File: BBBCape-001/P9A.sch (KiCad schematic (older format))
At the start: 29 parts, among them J1 addr, J3 CONN_6, J4 CONN_3, J5 CONN_3, J7 CONN_3, J8 CONN_4, Q2 BSS138, Q3 BSS138, Q4 BSS138, Q7 BSS138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

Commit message: Got GVS hooked up
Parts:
- removed U2: CAT24C256, SO8E, symbol CAT24C256
- added U2: CAT24C256, SO8E, symbol 24C512
- BRD1: renamed from U?; footprint ~ -> BEAGLEBONE
- J1: value addr -> ADR SEL
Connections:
- net labels added: GNDA_ADC, VDD_ADC
- wire segments 124 -> 122
- no-connect marks 1 -> 0
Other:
- moved on the sheet: BRD1C, C1, J1, R3, R4, R5

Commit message: CAPE UPS
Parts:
- removed J3: CONN_6, PIN_ARRAY-6X1, symbol CONN_6
- added F1: FUSE, SM1206, symbol FUSE
- added J10, J11, J12, J3: CONN_3, PIN_ARRAY_3X1, symbol CONN_3
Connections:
- net labels added: VDD_5V-UF
- wire segments 122 -> 132
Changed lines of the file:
@@
-EESchema Schematic File Version 2  date 24/06/2014 16:39:12
+EESchema Schematic File Version 2  date 25/06/2014 16:57:40
 LIBS:power
 LIBS:device
@@
 Sheet 2 6
 Title "BeagleBone Cape Baseline"
-Date "24 jun 2014"
+Date "25 jun 2014"
 Rev "X1"
 Comp "Doug Gilliland <doug@douglasgilliland.com>"
@@
 SYS_5V
 Text Label 5000 1300 0    60   ~ 0
-VDD_5V
+VDD_5V-UF
 Text Label 5000 3200 0    60   ~ 0
 DGND_9_2
@@
 Text Notes 3350 6700 0    60   ~ 0
 G\nV\nS
-Text Label 2800 10050 0    60   ~ 0
+Text Label 8350 2400 0    60   ~ 0
 AIN0
-Text Label 2800 9950 0    60   ~ 0
+Text Label 8350 2050 0    60   ~ 0
 AIN2
-Text Label 2800 9850 0    60   ~ 0
+Text Label 8350 1350 0    60   ~ 0
 AIN6
-Text Label 2800 9750 0    60   ~ 0
+Text Label 8350 1700 0    60   ~ 0
 AIN4
 Wire Wire Line
@@
 Wire Wire Line
 	2750 6650 2750 6950
-Wire Wire Line
-	3300 10050 2650 10050
-Wire Wire Line
-	3300 9950 2650 9950
-Wire Wire Line
-	3300 9850 2650 9850
-Wire Wire Line
-	3300 9750 2650 9750
-Wire Wire Line
-	3300 10150 2650 10150
-Wire Wire Line
-	2650 9650 3300 9650
 Text Label 1250 8050 0    60   ~ 0
 UART4_RXD
@@
 GP117
 $Comp
-L CONN_6 J3
-U 1 1 53A86882
-P 3650 9900
-F 0 "J3" V 3600 9900 60  0000 C CNN
-F 1 "CONN_6" V 3700 9900 60  0000 C CNN
-F 2 "PIN_ARRAY-6X1" H 3650 9550 60  0000 C CNN
-F 3 "" H 3650 9900 60  0000 C CNN
-	1    3650 9900
-	1    0    0    -1
-$EndComp
-$Comp
 L BEAGLEBONEBLACK BRD1
 U 3 1 53A89A26
@@
 Connection ~ 2800 3900
 Text GLabel 5000 1300 0    60   UnSpc ~ 0
-VDD_5V
+VDD_5V-UF
 Text GLabel 5000 3300 0    60   UnSpc ~ 0
 GND
-Text GLabel 2650 9650 0    60   UnSpc ~ 0
+Text GLabel 8200 1250 0    60   UnSpc ~ 0
 VDD_ADC
-Text GLabel 2650 10150 0    60   UnSpc ~ 0
+Text GLabel 8200 2200 0    60   UnSpc ~ 0
 GNDA_ADC
-Text Label 2800 9650 0    60   ~ 0
+Text Label 8350 1250 0    60   ~ 0
 VDD_ADC
 Text GLabel 5000 1900 0    60   UnSpc ~ 0
 I2C1_SCL
-Text Label 2800 10150 0    60   ~ 0
+Text Label 8350 2200 0    60   ~ 0
 GNDA_ADC
+Text GLabel 5000 1400 0    60   UnSpc ~ 0
+SYS_5V
+Wire Wire Line
+	8200 1250 9150 1250
+Wire Wire Line
+	9150 2300 9050 2300
+Wire Wire Line
+	9050 2300 9050 1250
+Connection ~ 9050 1250
+Wire Wire Line
+	9150 1600 9050 1600
+Connection ~ 9050 1600
+Wire Wire Line
+	9150 1950 9050 1950
+Connection ~ 9050 1950
+Wire Wire Line
+	9150 1150 8950 1150
+Wire Wire Line
+	8200 2200 9150 2200
+Connection ~ 8950 2200
+Wire Wire Line
+	9150 1850 8950 1850
+Connection ~ 8950 1850
+Wire Wire Line
+	8950 1150 8950 2200
+Wire Wire Line
+	9150 1500 8950 1500
+Connection ~ 8950 1500
+Wire Wire Line
+	9150 1350 8200 1350
+Wire Wire Line
+	9150 1700 8200 1700
+Wire Wire Line
+	9150 2050 8200 2050
+Wire Wire Line
+	9150 2400 8200 2400
+$Comp
+L CONN_3 J3
+U 1 1 53AACBAD
+P 9500 1250
+F 0 "J3" V 9450 1250 50  0000 C CNN
+F 1 "CONN_3" V 9550 1250 40  0000 C CNN
+F 2 "PIN_ARRAY_3X1" H 9550 1000 60  0000 C CNN
+F 3 "" H 9500 1250 60  0000 C CNN
+	1    9500 1250
+	1    0    0    -1
+$EndComp
+$Comp
+L CONN_3 J10
+U 1 1 53AACBB3
+P 9500 1600
+F 0 "J10" V 9450 1600 50  0000 C CNN
+F 1 "CONN_3" V 9550 1600 40  0000 C CNN
+F 2 "PIN_ARRAY_3X1" H 9550 1350 60  0000 C CNN
+F 3 "" H 9500 1600 60  0000 C CNN
+	1    9500 1600
+	1    0    0    -1
+$EndComp
+$Comp
+L CONN_3 J11
+U 1 1 53AACBB9
+P 9500 1950
+F 0 "J11" V 9450 1950 50  0000 C CNN
+F 1 "CONN_3" V 9550 1950 40  0000 C CNN
+F 2 "PIN_ARRAY_3X1" H 9550 1700 60  0000 C CNN
+F 3 "" H 9500 1950 60  0000 C CNN
+	1    9500 1950
+	1    0    0    -1
+$EndComp
+$Comp
+L CONN_3 J12
+U 1 1 53AACBC9
+P 9500 2300
+F 0 "J12" V 9450 2300 50  0000 C CNN
+F 1 "CONN_3" V 9550 2300 40  0000 C CNN
+F 2 "PIN_ARRAY_3X1" H 9550 2050 60  0000 C CNN
+F 3 "" H 9500 2300 60  0000 C CNN
+	1    9500 2300
+	1    0    0    -1
+$EndComp
+Text GLabel 4100 2300 2    60   UnSpc ~ 0
+I2C2_SDA
+$Comp
+L FUSE F1
+U 1 1 53AAD570
+P 4350 800
+F 0 "F1" H 4450 850 40  0000 C CNN
+F 1 "FUSE" H 4250 750 40  0000 C CNN
+F 2 "SM1206" H 4350 650 60  0000 C CNN
+F 3 "~" H 4350 800 60  0000 C CNN
+	1    4350 800
+	1    0    0    -1
+$EndComp
+Text Label 4700 800  0    60   ~ 0
+VDD_5V-UF
+Text Label 3700 800  0    60   ~ 0
+VDD_5V
+Wire Wire Line
+	4600 800  5350 800
+Wire Wire Line
+	4100 800  3600 800
+Text GLabel 3600 800  0    60   UnSpc ~ 0
+VDD_5V
 $EndSCHEMATC

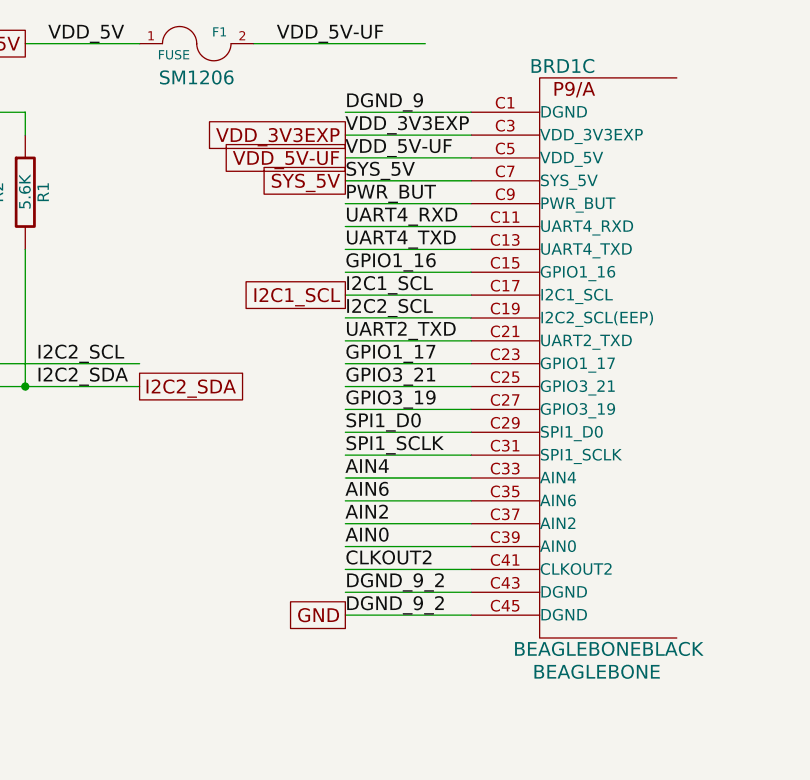
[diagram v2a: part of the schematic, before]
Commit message: New version, easier assembly
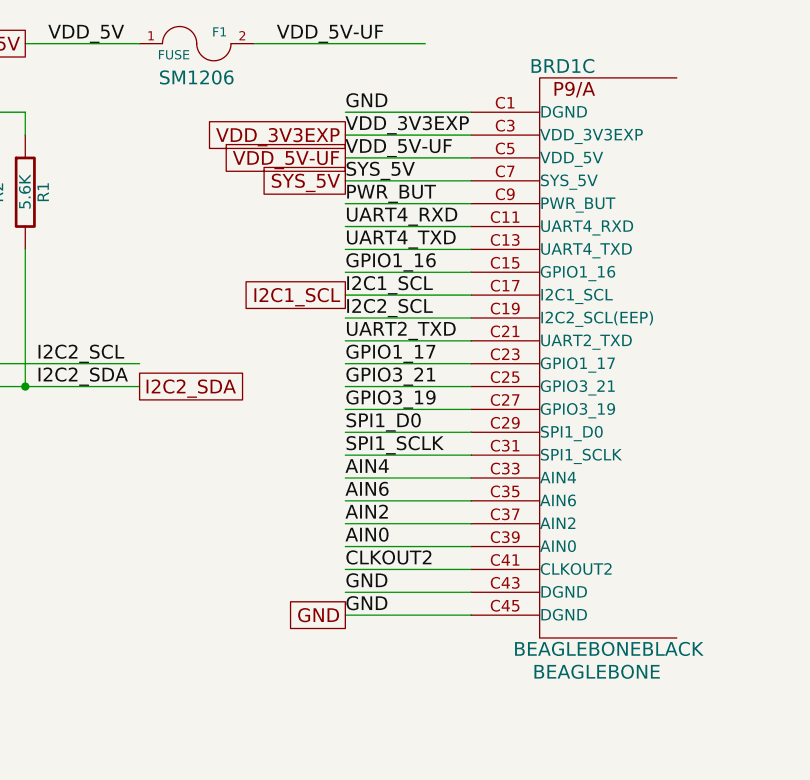
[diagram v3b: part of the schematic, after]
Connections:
- net labels removed: DGND_9, DGND_9_2
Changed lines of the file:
@@
-EESchema Schematic File Version 2  date 25/06/2014 16:57:40
+EESchema Schematic File Version 2  date 26/06/2014 11:29:44
 LIBS:power
 LIBS:device
@@
 Sheet 2 6
 Title "BeagleBone Cape Baseline"
-Date "25 jun 2014"
+Date "26 jun 2014"
 Rev "X1"
 Comp "Doug Gilliland <doug@douglasgilliland.com>"
@@
 VDD_5V-UF
 Text Label 5000 3200 0    60   ~ 0
-DGND_9_2
+GND
 Text Label 5000 3300 0    60   ~ 0
-DGND_9_2
+GND
 Text Label 5000 1100 0    60   ~ 0
-DGND_9
+GND
 Text Label 5000 1200 0    60   ~ 0
 VDD_3V3EXP
